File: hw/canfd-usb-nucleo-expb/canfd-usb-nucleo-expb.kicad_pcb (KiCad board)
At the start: 2 copper layers, 70 x 59 mm, 3 parts, among them J1 Conn_02x19_Odd_Even, J2 Conn_02x19_Odd_Even

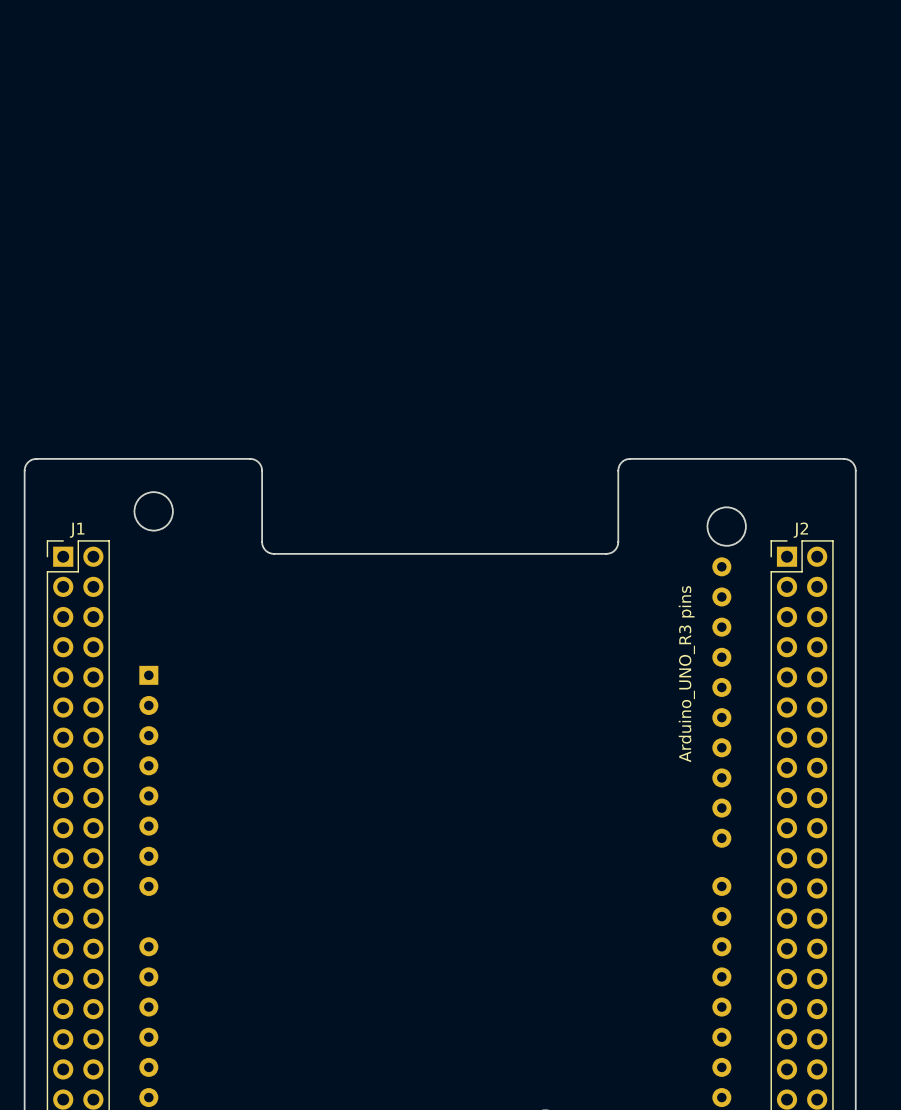
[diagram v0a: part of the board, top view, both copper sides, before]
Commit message: HW: Schematic edit - buttons and LEDs
Added buttons and LEDs to schematic, minor fixes in
existing components. Assigned most components with
their respective footprints.

Signed-off-by: AlexeyZ <silkt207@gmail.com>
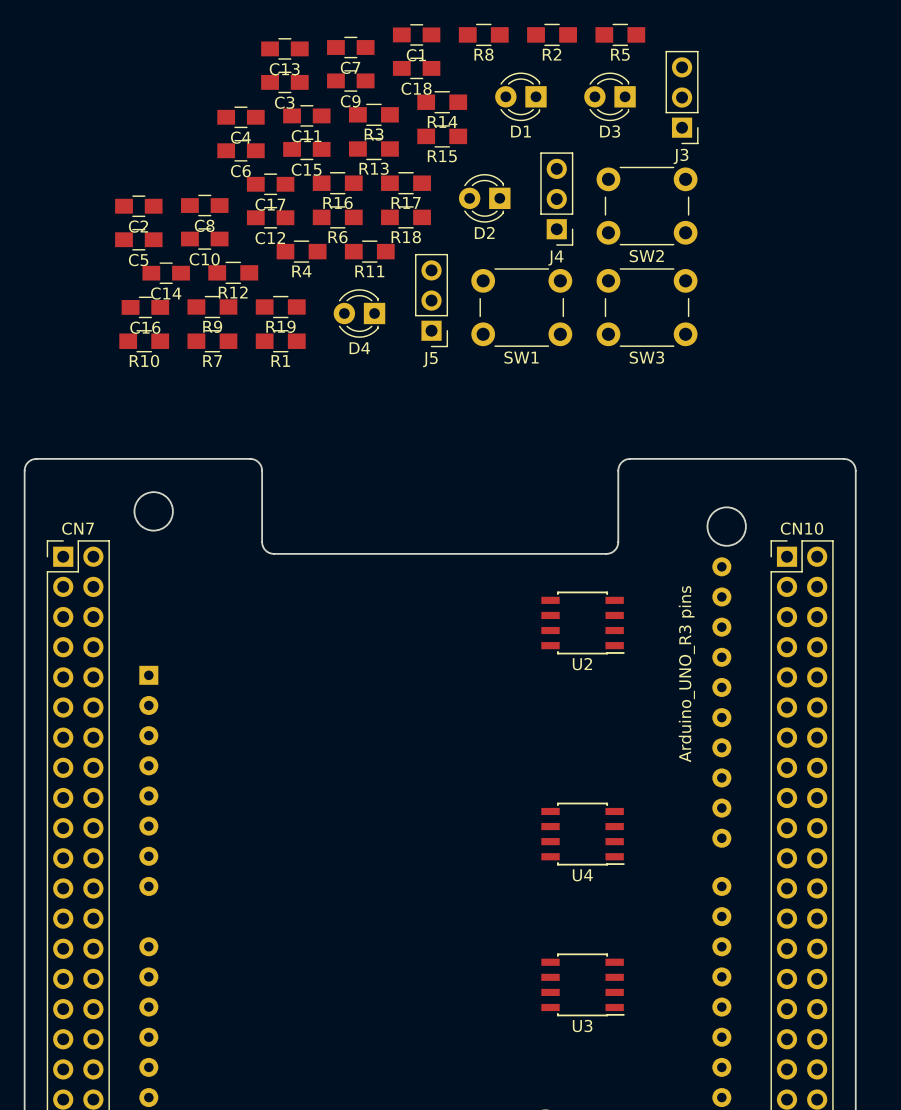
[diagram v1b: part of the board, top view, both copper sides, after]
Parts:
- removed J1, J2: Conn_02x19_Odd_Even, Pin_Headers:Pin_Header_Straight_2x19_Pitch2.54mm
- added C1: 100n, Capacitors_SMD:C_0805_HandSoldering, F.Cu at (135.3, 34.2)
- added C10: 100p, Capacitors_SMD:C_0805_HandSoldering, F.Cu at (117.4, 51.4)
- added C11: 100p, Capacitors_SMD:C_0805_HandSoldering, F.Cu at (126.0, 41.0)
- added C12: 100p, Capacitors_SMD:C_0805_HandSoldering, F.Cu at (123.0, 49.6)
- added C13: 4.7n, Capacitors_SMD:C_0805_HandSoldering, F.Cu at (124.2, 35.3)
- added C14: 4.7n, Capacitors_SMD:C_0805_HandSoldering, F.Cu at (114.2, 54.2)
- added C15: 4.7n, Capacitors_SMD:C_0805_HandSoldering, F.Cu at (126.0, 43.8)
- added C16: 100n, Capacitors_SMD:C_0805_HandSoldering, F.Cu at (112.4, 57.1)
- added C17: 100n, Capacitors_SMD:C_0805_HandSoldering, F.Cu at (123.0, 46.7)
- added C18: 100n, Capacitors_SMD:C_0805_HandSoldering, F.Cu at (135.3, 37.0)
- added C2: 100n, Capacitors_SMD:C_0805_HandSoldering, F.Cu at (111.9, 48.6)
- added C3: 100n, Capacitors_SMD:C_0805_HandSoldering, F.Cu at (124.2, 38.2)
- added C4: 15p, Capacitors_SMD:C_0805_HandSoldering, F.Cu at (120.5, 41.1)
- added C5: 15p, Capacitors_SMD:C_0805_HandSoldering, F.Cu at (111.9, 51.4)
- added C6: 15p, Capacitors_SMD:C_0805_HandSoldering, F.Cu at (120.5, 43.9)
- added C7: 100n, Capacitors_SMD:C_0805_HandSoldering, F.Cu at (129.7, 35.2)
- added C8: 100n, Capacitors_SMD:C_0805_HandSoldering, F.Cu at (117.4, 48.5)
- added C9: 100n, Capacitors_SMD:C_0805_HandSoldering, F.Cu at (129.7, 38.0)
- added CN10: CONN, Pin_Headers:Pin_Header_Straight_2x19_Pitch2.54mm, F.Cu at (166.4, 78.1)
- added CN7: POWER, Pin_Headers:Pin_Header_Straight_2x19_Pitch2.54mm, F.Cu at (105.5, 78.1)
- added D1: HEARTBEAT, LEDs:LED_D3.0mm, F.Cu at (145.3, 39.4)
- added D2: STATUS1, LEDs:LED_D3.0mm, F.Cu at (142.3, 47.9)
- added D3: STATUS2, LEDs:LED_D3.0mm, F.Cu at (152.8, 39.4)
- added D4: STATUS3, LEDs:LED_D3.0mm, F.Cu at (131.7, 57.6)
- added J3: Conn_01x03, Pin_Headers:Pin_Header_Straight_1x03_Pitch2.54mm, F.Cu at (157.6, 42.0)
- added J4: Conn_01x03, Pin_Headers:Pin_Header_Straight_1x03_Pitch2.54mm, F.Cu at (147.1, 50.5)
- added J5: Conn_01x03, Pin_Headers:Pin_Header_Straight_1x03_Pitch2.54mm, F.Cu at (136.5, 59.1)
- added R1: 62R, Resistors_SMD:R_0805_HandSoldering, F.Cu at (123.8, 60.0)
- added R10: 62R, Resistors_SMD:R_0805_HandSoldering, F.Cu at (112.3, 60.0)
- added R11: 62R, Resistors_SMD:R_0805_HandSoldering, F.Cu at (131.3, 52.4)
- added R12: 100k, Resistors_SMD:R_0805_HandSoldering, F.Cu at (119.8, 54.2)
- added R13: 100k, Resistors_SMD:R_0805_HandSoldering, F.Cu at (131.7, 43.8)
- added R14: 100k, Resistors_SMD:R_0805_HandSoldering, F.Cu at (137.4, 39.8)
- added R15: 100k, Resistors_SMD:R_0805_HandSoldering, F.Cu at (137.4, 42.7)
- added R16: 100k, Resistors_SMD:R_0805_HandSoldering, F.Cu at (128.6, 46.7)
- added R17: 100k, Resistors_SMD:R_0805_HandSoldering, F.Cu at (134.4, 46.7)
- added R18: 100k, Resistors_SMD:R_0805_HandSoldering, F.Cu at (134.4, 49.5)
- added R19: 100k, Resistors_SMD:R_0805_HandSoldering, F.Cu at (123.8, 57.1)
- added R2: 62R, Resistors_SMD:R_0805_HandSoldering, F.Cu at (146.7, 34.2)
- added R3: 62R, Resistors_SMD:R_0805_HandSoldering, F.Cu at (131.7, 40.9)
- added R4: 62R, Resistors_SMD:R_0805_HandSoldering, F.Cu at (125.6, 52.4)
- added R5: 62R, Resistors_SMD:R_0805_HandSoldering, F.Cu at (152.4, 34.2)
- added R6: 62R, Resistors_SMD:R_0805_HandSoldering, F.Cu at (128.6, 49.5)
- added R7: 62R, Resistors_SMD:R_0805_HandSoldering, F.Cu at (118.1, 60.0)
- added R8: 62R, Resistors_SMD:R_0805_HandSoldering, F.Cu at (140.9, 34.2)
- added R9: 62R, Resistors_SMD:R_0805_HandSoldering, F.Cu at (118.1, 57.1)
- added SW1: SW_Push_Dual_x2, Buttons_Switches_THT:SW_PUSH_6mm, F.Cu at (147.4, 59.4)
- added SW2: SW_Push_Dual_x2, Buttons_Switches_THT:SW_PUSH_6mm, F.Cu at (157.9, 50.8)
- added SW3: SW_Push_Dual_x2, Buttons_Switches_THT:SW_PUSH_6mm, F.Cu at (157.9, 59.4)
- added U2: ATA6561-GAQW-N, Housings_SOIC:SOIC-8_3.9x4.9mm_Pitch1.27mm, F.Cu at (149.2, 83.7)
- added U3: ATA6561-GAQW-N, Housings_SOIC:SOIC-8_3.9x4.9mm_Pitch1.27mm, F.Cu at (149.2, 114.2)
- added U4: ATA6561-GAQW-N, Housings_SOIC:SOIC-8_3.9x4.9mm_Pitch1.27mm, F.Cu at (149.2, 101.5)

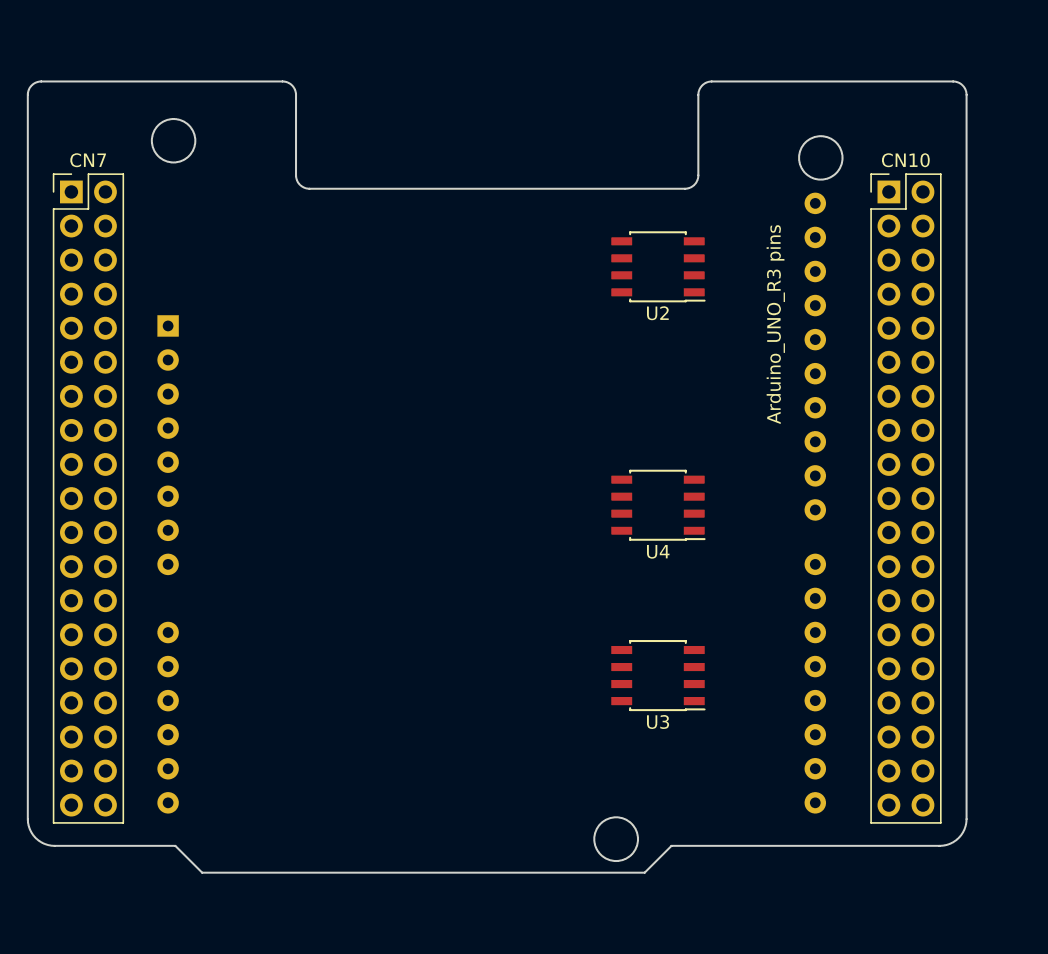
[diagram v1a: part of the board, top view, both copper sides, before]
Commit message: HW: Schematic fixes, PCB outline fixes
1. PCB outline is now a rectangle, arduino pins are removed
2. 22u tantalum cap added on 5V rail
3. USB termination resistors are removed as they are implemented
in MCU's PHY
4. Buttons are stronger pulled-up with 10k resistors instead of
100k like on other stm boards, 100 Ohm resistors added in series
with debouncing caps
5.Placeholder components remowed
6.Shielding through 220k resistor with 10n cap
7.ESD protection connection fixed
8.USB Type-C instead of Mini-B
9. Replaced standby mode jumpers with solder-jumpers for choosing
between always normal mode or controlled through MCU. Current-limiting
resistors added on standby lines.

Co-authored-by: Viacheslav Olizarenko <stiwenss@gmail.com>
Co-authored-by: AlexeyZ <silkt207@gmail.com>
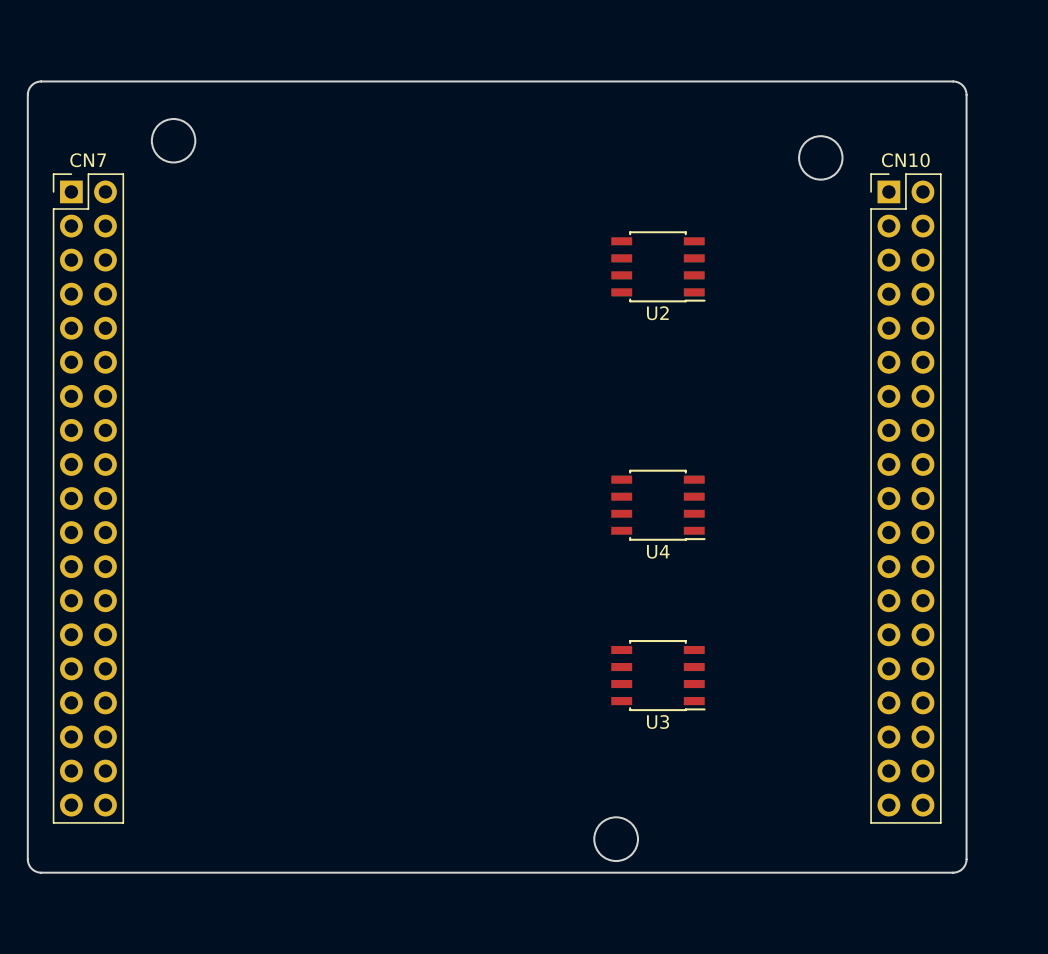
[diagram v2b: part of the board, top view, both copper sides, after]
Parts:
- removed Arduino_UNO_R3 pins: Arduino_UNO_R3_pins, Modules:Arduino_UNO_R3
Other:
- outline, holes or cut-outs redrawn
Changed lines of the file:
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@@
   (general
     (thickness 1.6)
-    (drawings 24)
+    (drawings 12)
     (tracks 0)
     (zones 0)
-    (modules 53)
+    (modules 52)
     (nets 38)
   )
@@
     )
   )
-  (module Modules:Arduino_UNO_R3 (layer B.Cu)
-    (at 112.695 88.103 270)
-    (descr "Arduino UNO R3, http://www.mouser.com/pdfdocs/Gravitech_Arduino_Nano3_0.pdf")
-    (tags "Arduino UNO R3")
-    (fp_text reference "Arduino_UNO_R3 pins" (at -0.127 -45.212 90) (layer F.SilkS)
-      (effects (font (size 1 1) (thickness 0.15)))
-    )
-    (fp_text value Arduino_UNO_R3_pins (at 6.985 -2.159 90) (layer F.Fab)
-      (effects (font (size 1 1) (thickness 0.15)))
-    )
-    (pad 16 thru_hole oval (at 33.02 -48.26 180) (size 1.6 1.6) (drill 0.8) (layers *.Cu *.Mask))
-    (pad 15 thru_hole oval (at 35.56 -48.26 180) (size 1.6 1.6) (drill 0.8) (layers *.Cu *.Mask))
-    (pad 30 thru_hole oval (at -4.06 -48.26 180) (size 1.6 1.6) (drill 0.8) (layers *.Cu *.Mask))
-    (pad 14 thru_hole oval (at 35.56 0 180) (size 1.6 1.6) (drill 0.8) (layers *.Cu *.Mask))
-    (pad 29 thru_hole oval (at -1.52 -48.26 180) (size 1.6 1.6) (drill 0.8) (layers *.Cu *.Mask))
-    (pad 13 thru_hole oval (at 33.02 0 180) (size 1.6 1.6) (drill 0.8) (layers *.Cu *.Mask))
-    (pad 28 thru_hole oval (at 1.02 -48.26 180) (size 1.6 1.6) (drill 0.8) (layers *.Cu *.Mask))
-    (pad 12 thru_hole oval (at 30.48 0 180) (size 1.6 1.6) (drill 0.8) (layers *.Cu *.Mask))
-    (pad 27 thru_hole oval (at 3.56 -48.26 180) (size 1.6 1.6) (drill 0.8) (layers *.Cu *.Mask))
-    (pad 11 thru_hole oval (at 27.94 0 180) (size 1.6 1.6) (drill 0.8) (layers *.Cu *.Mask))
-    (pad 26 thru_hole oval (at 6.1 -48.26 180) (size 1.6 1.6) (drill 0.8) (layers *.Cu *.Mask))
-    (pad 10 thru_hole oval (at 25.4 0 180) (size 1.6 1.6) (drill 0.8) (layers *.Cu *.Mask))
-    (pad 25 thru_hole oval (at 8.64 -48.26 180) (size 1.6 1.6) (drill 0.8) (layers *.Cu *.Mask))
-    (pad 9 thru_hole oval (at 22.86 0 180) (size 1.6 1.6) (drill 0.8) (layers *.Cu *.Mask))
-    (pad 24 thru_hole oval (at 11.18 -48.26 180) (size 1.6 1.6) (drill 0.8) (layers *.Cu *.Mask))
-    (pad 8 thru_hole oval (at 17.78 0 180) (size 1.6 1.6) (drill 0.8) (layers *.Cu *.Mask))
-    (pad 23 thru_hole oval (at 13.72 -48.26 180) (size 1.6 1.6) (drill 0.8) (layers *.Cu *.Mask))
-    (pad 7 thru_hole oval (at 15.24 0 180) (size 1.6 1.6) (drill 0.8) (layers *.Cu *.Mask))
-    (pad 22 thru_hole oval (at 17.78 -48.26 180) (size 1.6 1.6) (drill 0.8) (layers *.Cu *.Mask))
-    (pad 6 thru_hole oval (at 12.7 0 180) (size 1.6 1.6) (drill 0.8) (layers *.Cu *.Mask))
-    (pad 21 thru_hole oval (at 20.32 -48.26 180) (size 1.6 1.6) (drill 0.8) (layers *.Cu *.Mask))
-    (pad 5 thru_hole oval (at 10.16 0 180) (size 1.6 1.6) (drill 0.8) (layers *.Cu *.Mask))
-    (pad 20 thru_hole oval (at 22.86 -48.26 180) (size 1.6 1.6) (drill 0.8) (layers *.Cu *.Mask))
-    (pad 4 thru_hole oval (at 7.62 0 180) (size 1.6 1.6) (drill 0.8) (layers *.Cu *.Mask))
-    (pad 19 thru_hole oval (at 25.4 -48.26 180) (size 1.6 1.6) (drill 0.8) (layers *.Cu *.Mask))
-    (pad 3 thru_hole oval (at 5.08 0 180) (size 1.6 1.6) (drill 0.8) (layers *.Cu *.Mask))
-    (pad 18 thru_hole oval (at 27.94 -48.26 180) (size 1.6 1.6) (drill 0.8) (layers *.Cu *.Mask))
-    (pad 2 thru_hole oval (at 2.54 0 180) (size 1.6 1.6) (drill 0.8) (layers *.Cu *.Mask))
-    (pad 17 thru_hole oval (at 30.48 -48.26 180) (size 1.6 1.6) (drill 0.8) (layers *.Cu *.Mask))
-    (pad 1 thru_hole rect (at 0 0 180) (size 1.6 1.6) (drill 0.8) (layers *.Cu *.Mask))
-    (pad 31 thru_hole oval (at -6.6 -48.26 180) (size 1.6 1.6) (drill 0.8) (layers *.Cu *.Mask))
-    (pad 32 thru_hole oval (at -9.14 -48.26 180) (size 1.6 1.6) (drill 0.8) (layers *.Cu *.Mask))
-  )
+  (gr_line (start 171.235 128.873) (end 103.235 128.873) (layer Edge.Cuts) (width 0.15))
+  (gr_line (start 172.235 70.873) (end 172.235 127.873) (layer Edge.Cuts) (width 0.15))
+  (gr_line (start 102.235 127.873) (end 102.235 70.873) (layer Edge.Cuts) (width 0.15))
+  (gr_arc (start 103.235 127.873) (end 103.235 128.873) (angle 90) (layer Edge.Cuts) (width 0.15))
+  (gr_arc (start 171.235 127.873) (end 172.235 127.873) (angle 90) (layer Edge.Cuts) (width 0.15))
+  (gr_line (start 171.235 69.873) (end 103.235 69.873) (layer Edge.Cuts) (width 0.15))
+  (gr_circle (center 146.105 126.373) (end 147.735 126.373) (layer Edge.Cuts) (width 0.15))
   (gr_text "CAN FD Physical-layer expansion board\nfor NUCLEO-G474RE" (at 179.07 171.958) (layer F.Cu)
     (effects (font (size 2.5 1.7) (thickness 0.3)) (justify left))
   )
-  (gr_line (start 103.235 69.873) (end 121.235 69.873) (layer Edge.Cuts) (width 0.15))
-  (gr_line (start 104.235 126.873) (end 113.235 126.873) (layer Edge.Cuts) (width 0.15))
-  (gr_line (start 150.235 126.873) (end 170.235 126.873) (layer Edge.Cuts) (width 0.15))
-  (gr_line (start 113.235 126.873) (end 115.235 128.873) (layer Edge.Cuts) (width 0.15))
-  (gr_line (start 148.235 128.873) (end 150.235 126.873) (layer Edge.Cuts) (width 0.15))
-  (gr_line (start 115.235 128.873) (end 148.235 128.873) (layer Edge.Cuts) (width 0.15))
-  (gr_line (start 122.235 70.873) (end 122.235 76.873) (layer Edge.Cuts) (width 0.15))
-  (gr_line (start 102.235 124.873) (end 102.235 70.873) (layer Edge.Cuts) (width 0.15))
   (gr_arc (start 171.235 70.873) (end 171.235 69.873) (angle 90) (layer Edge.Cuts) (width 0.15))
-  (gr_arc (start 121.235 70.873) (end 121.235 69.873) (angle 90) (layer Edge.Cuts) (width 0.15))
-  (gr_line (start 151.235 77.873) (end 123.235 77.873) (layer Edge.Cuts) (width 0.15))
-  (gr_arc (start 123.235 76.873) (end 123.235 77.873) (angle 90) (layer Edge.Cuts) (width 0.15))
-  (gr_arc (start 153.235 70.873) (end 152.235 70.873) (angle 90) (layer Edge.Cuts) (width 0.15))
   (gr_arc (start 103.235 70.873) (end 102.235 70.873) (angle 90) (layer Edge.Cuts) (width 0.15))
-  (gr_arc (start 151.235 76.873) (end 152.235 76.873) (angle 90) (layer Edge.Cuts) (width 0.15))
-  (gr_arc (start 170.235 124.873) (end 172.235 124.873) (angle 90) (layer Edge.Cuts) (width 0.15))
-  (gr_line (start 172.235 124.873) (end 172.235 70.873) (layer Edge.Cuts) (width 0.15))
-  (gr_line (start 152.235 70.873) (end 152.235 76.873) (layer Edge.Cuts) (width 0.15))
-  (gr_line (start 171.235 69.873) (end 153.235 69.873) (layer Edge.Cuts) (width 0.15))
   (gr_circle (center 161.365 75.573) (end 162.985 75.573) (layer Edge.Cuts) (width 0.15))
-  (gr_circle (center 146.105 126.373) (end 147.735 126.373) (layer Edge.Cuts) (width 0.15))
-  (gr_arc (start 104.235 124.873) (end 104.235 126.873) (angle 90) (layer Edge.Cuts) (width 0.15))
   (gr_circle (center 113.105 74.293) (end 114.725 74.293) (layer Edge.Cuts) (width 0.15))
 )
